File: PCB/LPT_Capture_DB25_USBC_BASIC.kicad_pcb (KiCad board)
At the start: 2 copper layers, 36 x 22.8 mm, 18 parts, among them J1 GSB1C4621DS2HR, J2 DB25P064TXLF, U1 FT245RL

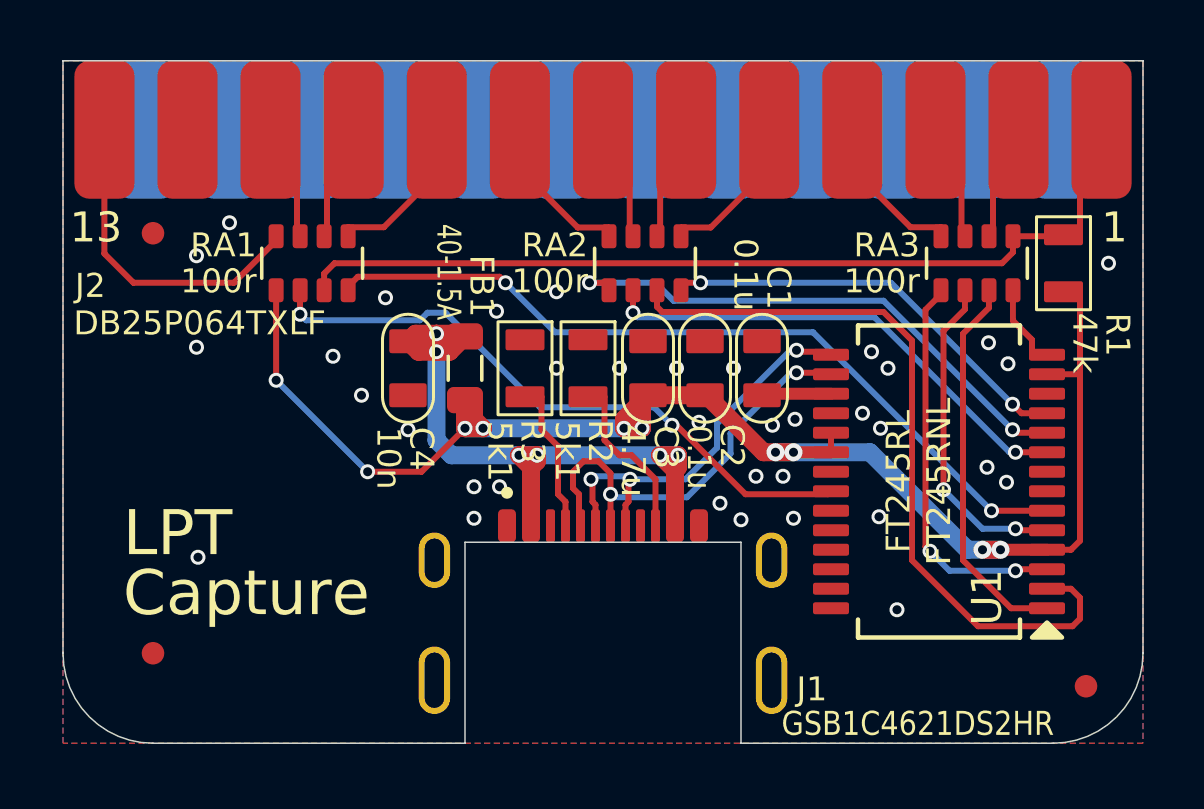
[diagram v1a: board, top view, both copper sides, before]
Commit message: pull c36_usbc_fancy into main
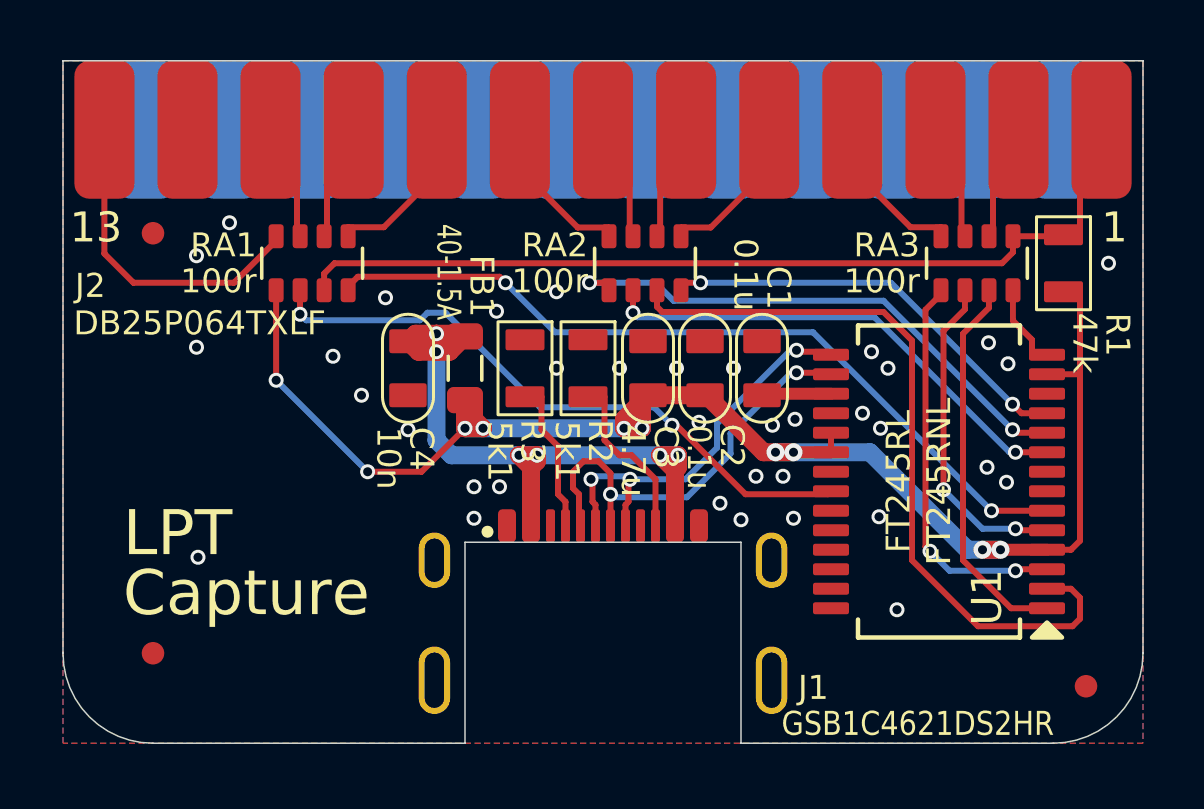
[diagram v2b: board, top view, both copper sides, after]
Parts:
- J1: footprint 000_LOCAL:USBC_16pin_mid_mount -> 000_LOCAL:USBC_Receptacle_16pin_mid_mount
